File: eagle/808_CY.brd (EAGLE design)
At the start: 100 x 80 mm, 112 parts, among them IC1 TL071P, IC2 TL071P, IC3 TL071P, IC4 TL072P, Q1 2N3904, Q2 2N3904, Q3 2N3904, Q4 2N3904, Q5 2N3904, Q6 2N3904, Q7 2N3904, Q8 2N3906

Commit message: third of the parts on
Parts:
- moved Q4 132.4 mm to (25.4, 45.7), turned to 90 degrees
- moved R96* 131.4 mm to (20.3, 45.7), turned to 90 degrees
- moved R98* 127.6 mm to (21.6, 50.8), turned to 180 degrees
- moved R58* 121.3 mm to (25.4, 31.8), turned to 270 degrees
- moved C44* 113.9 mm to (17.8, 38.1), turned to 90 degrees
- moved D11* 110.5 mm to (15.2, 57.1), turned to 90 degrees
- moved C46* 109.7 mm to (6.35, 41.9)
- moved C42* 108.9 mm to (20.3, 38.1), turned to 90 degrees
- moved R95* 106.3 mm to (25.4, 39.4), turned to 270 degrees
- moved C36* 96.9 mm to (26.7, 50.8), turned to 90 degrees
- moved C43* 89.3 mm to (12.7, 50.8), turned to 270 degrees
- moved C16* 85.9 mm to (21.6, 30.5), turned to 180 degrees
- moved Q1 81.8 mm to (8.89, 48.3), turned to 90 degrees
- moved R55* 81.3 mm to (15.2, 26.7)
- moved C15* 79.2 mm to (21.6, 33.0)
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
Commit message: third of the parts on
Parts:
- moved R94* 122.9 mm to (24.1, 59.7)
- moved C50* 121.5 mm to (19.1, 55.9), turned to 90 degrees
- moved C47* 107.6 mm to (24.1, 55.9), turned to 180 degrees
- moved C40* 106.8 mm to (15.2, 71.1)
- moved Q2 102.1 mm to (31.8, 73.7)
- moved C48* 98.8 mm to (3.81, 76.2), turned to 90 degrees
- moved C38* 97.8 mm to (16.5, 66.0), turned to 90 degrees
- moved C59* 97.4 mm to (26.7, 77.5)
- moved R91* 95.6 mm to (20.3, 66.0), turned to 270 degrees
- moved R127* 90.7 mm to (36.8, 74.9), turned to 270 degrees
- moved R87* 87.6 mm to (25.4, 62.2)
- moved R88* 80.2 mm to (11.4, 66.0), turned to 270 degrees
- moved R126* 77.7 mm to (31.8, 69.8)
- moved D7* 69.7 mm to (8.89, 72.4), turned to 90 degrees
- moved C45* 68.6 mm to (7.62, 63.5)
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
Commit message: parts on the board
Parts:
- moved R15* 202.5 mm to (92.7, 22.9), turned to 90 degrees
- moved R10* 189.8 mm to (82.5, 12.7)
- moved R6* 183.3 mm to (86.4, 20.3)
- moved Q3 177.4 mm to (74.9, 16.5), turned to 180 degrees
- moved R3* 176.8 mm to (91.4, 31.8), turned to 90 degrees
- moved R121* 175.5 mm to (71.1, 26.7), turned to 180 degrees
- moved R86* 173.9 mm to (74.9, 43.2), turned to 90 degrees
- moved C41* 168.1 mm to (63.5, 34.3), turned to 270 degrees
- moved R93* 164.9 mm to (68.6, 38.1)
- moved R92* 162.0 mm to (69.8, 30.5)
- moved R114* 158.3 mm to (48.3, 24.1), turned to 270 degrees
- moved D8* 156.6 mm to (77.5, 36.8)
- moved R120* 156.1 mm to (57.1, 20.3)
- moved Q7 154.6 mm to (85.1, 35.6), turned to 270 degrees
- moved Q8 154.3 mm to (88.9, 15.2), turned to 90 degrees
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
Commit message: 90 pct routed
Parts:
- R100*, R101*, R110*: device TR808clone:0207/2V -> TR808clone:0207/7
- R115*: device TR808clone:0207/5V -> TR808clone:0207/7
- moved R105* 49.6 mm to (88.9, 27.9), turned to 180 degrees
- moved PWR1 38.1 mm to (92.7, 16.5)
- moved R10* 36.1 mm to (47.0, 6.35), turned to 270 degrees
- moved R15* 27.9 mm to (72.4, 3.81), turned to 0 degrees
- moved R121* 26.7 mm to (47.0, 15.2)
- moved R112* 22.5 mm to (12.7, 48.3), turned to 180 degrees
- moved Q3 21.3 mm to (54.6, 10.2), turned to 270 degrees
- moved R123* 20.7 mm to (58.4, 19.1)
- moved R3* 20.1 mm to (80.0, 15.2), turned to 0 degrees
- moved DIGINOISE_NORM 19.1 mm to (15.2, 63.5)
- moved R118* 18.2 mm to (33.0, 20.3), turned to 0 degrees
- moved C55* 17.3 mm to (21.6, 45.7)
- moved C16* 16.9 mm to (22.9, 54.6)
- moved R59* 16.9 mm to (24.1, 58.4)
- moved Q8 16.1 mm to (73.7, 10.2)
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
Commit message: tweaks
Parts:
- R106*, R109*, R89*, R98*: device TR808clone:0207/2V -> TR808clone:0207/5V
- R113*, R86*: device TR808clone:0207/2V -> TR808clone:0207/7
- moved R83* 5.39 mm to (66.0, 11.4), turned to 90 degrees
- moved R100* 4.02 mm to (40.6, 63.5)
- moved R113* 4.02 mm to (48.3, 34.3), turned to 0 degrees
- moved R3* 4.02 mm to (81.3, 11.4), turned to 270 degrees
- moved Q5 2.84 mm to (50.8, 61.0)
- moved R128* 2.84 mm to (31.8, 5.08)
- moved R86* 2.84 mm to (76.2, 40.6)
- moved C50* 1.80 mm to (66.0, 61.0)
- moved D12* 1.80 mm to (63.5, 74.9)
- moved R109* 1.80 mm to (44.5, 48.3)
- moved C39* 1.27 mm to (64.8, 71.1), turned to 90 degrees
- moved D5* 1.27 mm to (61.0, 52.1)
- moved Q4 1.27 mm to (50.8, 52.1)
- moved R111* 1.27 mm to (41.9, 41.9)
- moved R93* 1.27 mm to (68.6, 36.8)
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
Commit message: tweaks
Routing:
- net GND: track 0.00 -> 549.4 mm
- net -15V: track 0.00 -> 168.9 mm
- net +15V: track 0.00 -> 156.7 mm
- net N$546: track 0.00 -> 79.0 mm
- net N$558: track 0.00 -> 70.6 mm
- net N$223: track 0.00 -> 59.3 mm
- net N$544: track 0.00 -> 54.5 mm
- net N$177: track 0.00 -> 47.6 mm
- net TO_HH: track 0.00 -> 41.0 mm
- net TRIG*: track 0.00 -> 34.2 mm
- net N$517: track 0.00 -> 33.2 mm
- net N$508: track 0.00 -> 30.8 mm
- net N$498: track 0.00 -> 30.1 mm
- net N$516: track 0.00 -> 30.0 mm
- net N$503: track 0.00 -> 28.8 mm
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
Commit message: tweaks
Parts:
- D5*: value 1N4148DO35-7 -> 1N4148DO35-10; device TR808clone:DO35-7 -> TR808clone:DO35-10
- R102*, R58*: device TR808clone:0207/2V -> TR808clone:0207/7
- R55*, R95*: device TR808clone:0207/5V -> TR808clone:0207/7
- R90*: device TR808clone:0207/2V -> TR808clone:0207/5V
- moved C58* 20.4 mm to (77.5, 44.5), turned to 180 degrees
- moved R85* 18.3 mm to (78.7, 34.3), turned to 0 degrees
- moved R6* 18.2 mm to (57.1, 10.2), turned to 270 degrees
- moved D8* 17.8 mm to (94.0, 33.0), turned to 90 degrees
- moved R3* 17.7 mm to (64.8, 5.08)
- moved R105* 15.5 mm to (73.7, 25.4), turned to 270 degrees
- moved R104* 14.0 mm to (85.1, 76.2), turned to 180 degrees
- moved R108* 11.7 mm to (40.6, 35.6)
- moved R123* 11.4 mm to (69.8, 19.1)
- moved R102* 10.9 mm to (45.7, 68.6)
- moved R93* 10.2 mm to (59.7, 31.8)
- moved R10* 10.2 mm to (57.1, 5.08), turned to 0 degrees
- moved R115* 10.2 mm to (24.1, 35.6), turned to 0 degrees
- moved Q6 7.73 mm to (80.0, 27.9)
- moved R56* 7.41 mm to (39.4, 67.3), turned to 0 degrees
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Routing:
- net -15V: track 168.9 -> 2.54 mm
- net +15V: track 156.7 -> 31.4 mm
- net N$528: track 8.98 -> 59.9 mm
- net N$529: track 8.78 -> 56.2 mm
- net N$548: track 7.93 -> 48.9 mm
- net N$546: track 79.0 -> 41.1 mm
- net N$553: track 0.00 -> 33.1 mm
- net N$515: track 9.42 -> 41.4 mm
- net N$513: track 28.2 -> 55.7 mm
- net N$544: track 54.5 -> 79.1 mm
- net N$539: track 8.10 -> 27.3 mm
- net N$177: track 47.6 -> 29.7 mm
- net N$517: track 33.2 -> 16.2 mm
- net N$524: track 25.9 -> 9.81 mm
- net CY: track 15.4 -> 30.4 mm
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
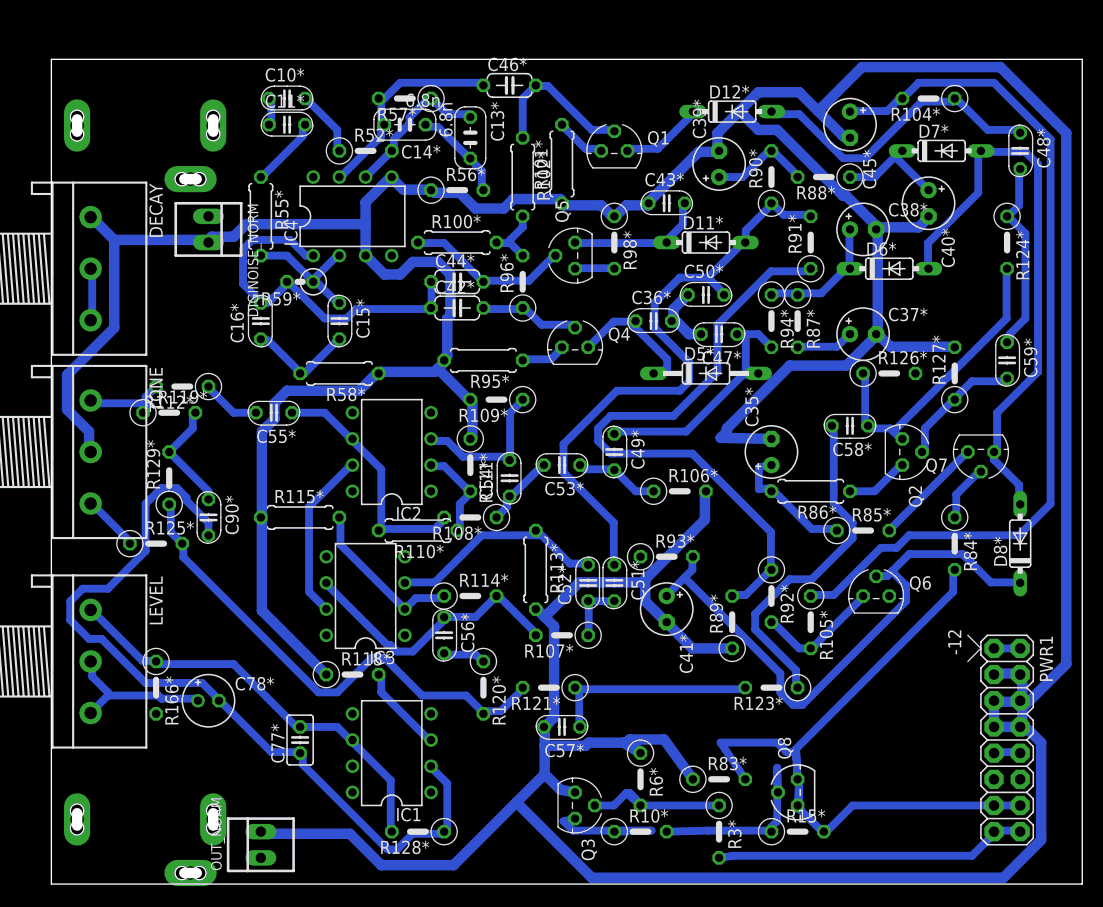
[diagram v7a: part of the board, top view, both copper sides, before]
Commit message: trying a smaller width
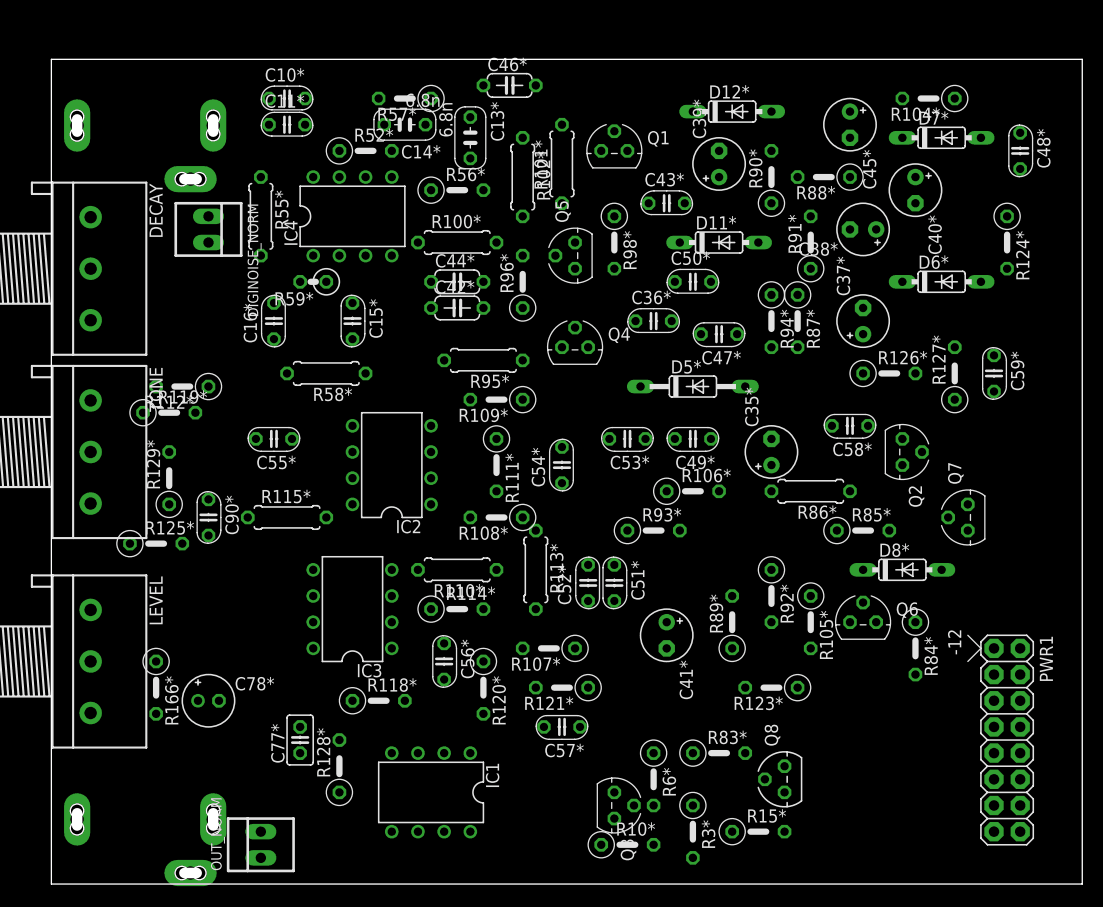
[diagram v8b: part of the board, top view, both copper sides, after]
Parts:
- moved D8* 11.7 mm to (82.5, 30.5), turned to 0 degrees
- moved R84* 10.9 mm to (83.8, 22.9)
- moved R128* 9.92 mm to (27.9, 11.4), turned to 90 degrees
- moved C49* 7.73 mm to (62.2, 43.2), turned to 180 degrees
- moved C53* 6.84 mm to (55.9, 43.2)
- moved Q7 6.48 mm to (88.9, 35.6), turned to 90 degrees
- moved IC1 5.39 mm to (36.8, 8.89), turned to 180 degrees
- moved R110* 5.39 mm to (39.4, 30.5)
- moved C54* 5.24 mm to (49.5, 40.6)
- moved D6* 5.24 mm to (86.4, 58.4)
- moved Q3 3.81 mm to (54.6, 7.62)
- moved R15* 3.81 mm to (68.6, 5.08)
- moved R118* 3.59 mm to (31.8, 17.8)
- moved Q6 2.84 mm to (78.7, 25.4)
- moved R93* 2.84 mm to (58.4, 34.3)
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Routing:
- net GND: track 540.0 -> 0.00 mm
- net N$558: track 85.2 -> 0.00 mm
- net N$544: track 79.1 -> 0.00 mm
- net N$223: track 60.2 -> 0.00 mm
- net N$528: track 59.9 -> 0.00 mm
- net N$529: track 56.2 -> 0.00 mm
- net N$513: track 55.7 -> 0.00 mm
- net N$548: track 48.9 -> 0.00 mm
- net N$515: track 41.4 -> 0.00 mm
- net N$546: track 41.1 -> 0.00 mm
- net TO_HH: track 35.6 -> 0.00 mm
- net N$553: track 33.1 -> 0.00 mm
- net +15V: track 31.4 -> 0.00 mm
- net CY: track 30.4 -> 0.00 mm
- net N$508: track 30.0 -> 0.00 mm
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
